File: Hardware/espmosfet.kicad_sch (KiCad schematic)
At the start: 59 parts, among them J1 USB_B_Micro, J2 Conn_01x04_Male, J3 USB_A, J4 Conn_01x04_Male, J5 Conn_01x02_Male, J6 Conn_01x02_Male, J7 Conn_01x03_Male, P1 USB_C_Receptacle_USB2.0, P2 USB_C_Receptacle_USB2.0, Q1 AO3400A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

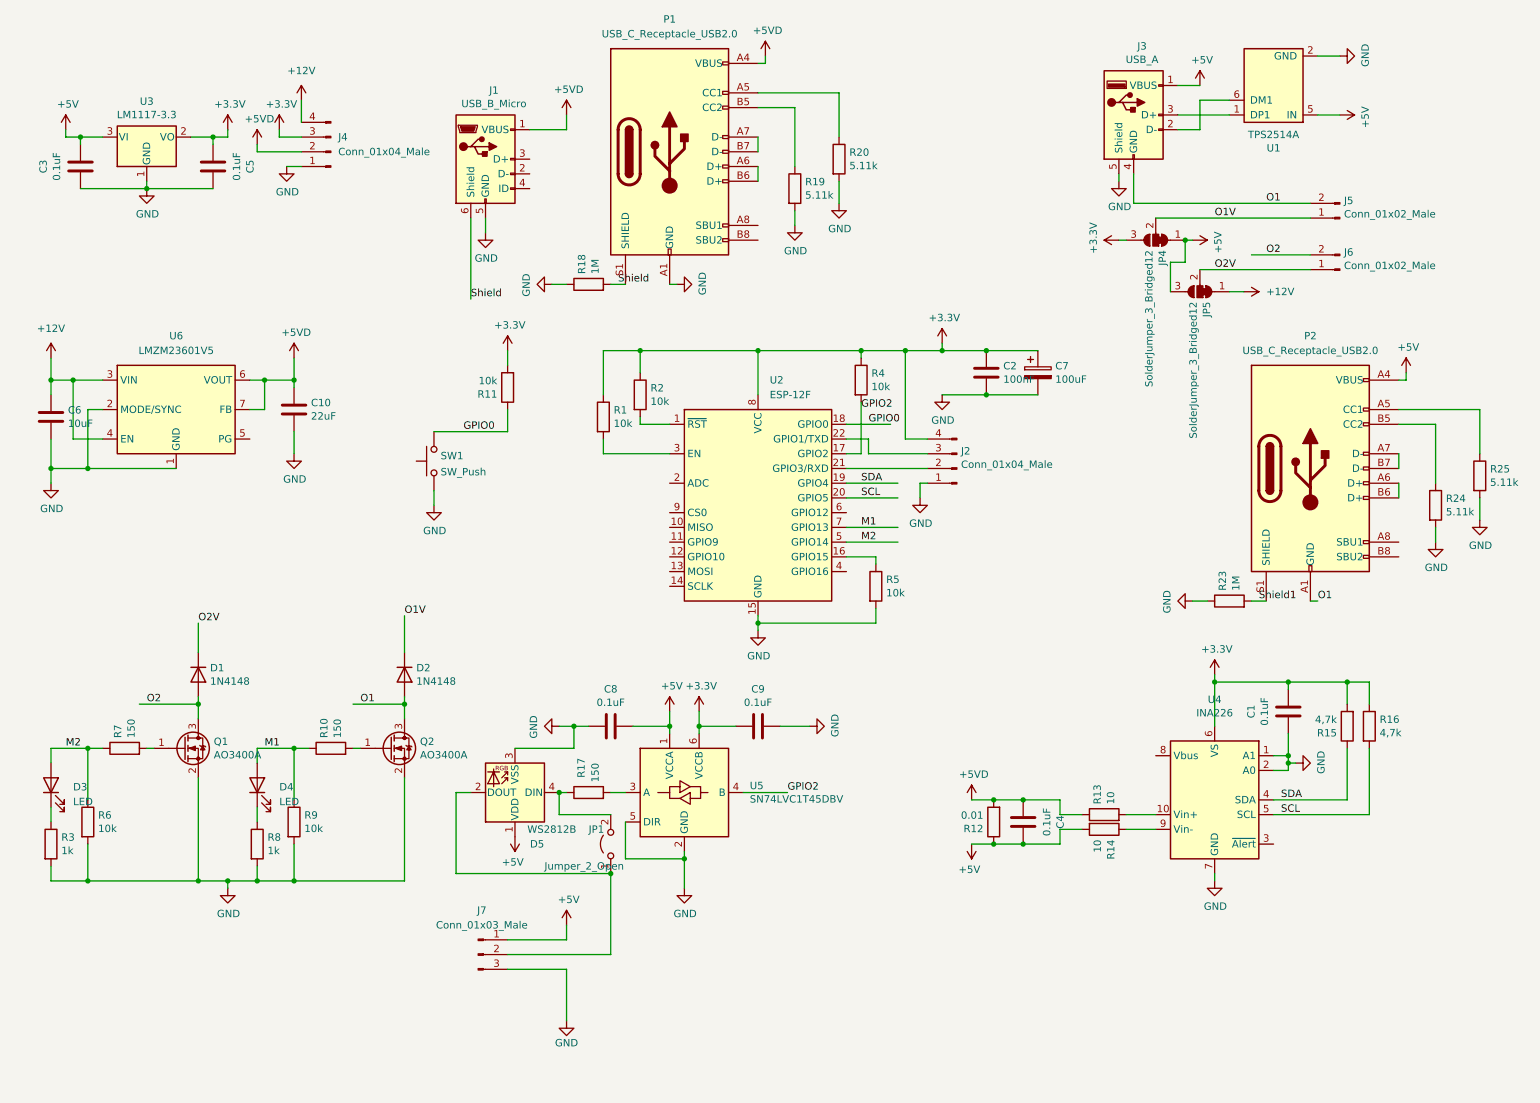
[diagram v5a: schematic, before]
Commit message: fix ws2812b pinout, change to open jumpers
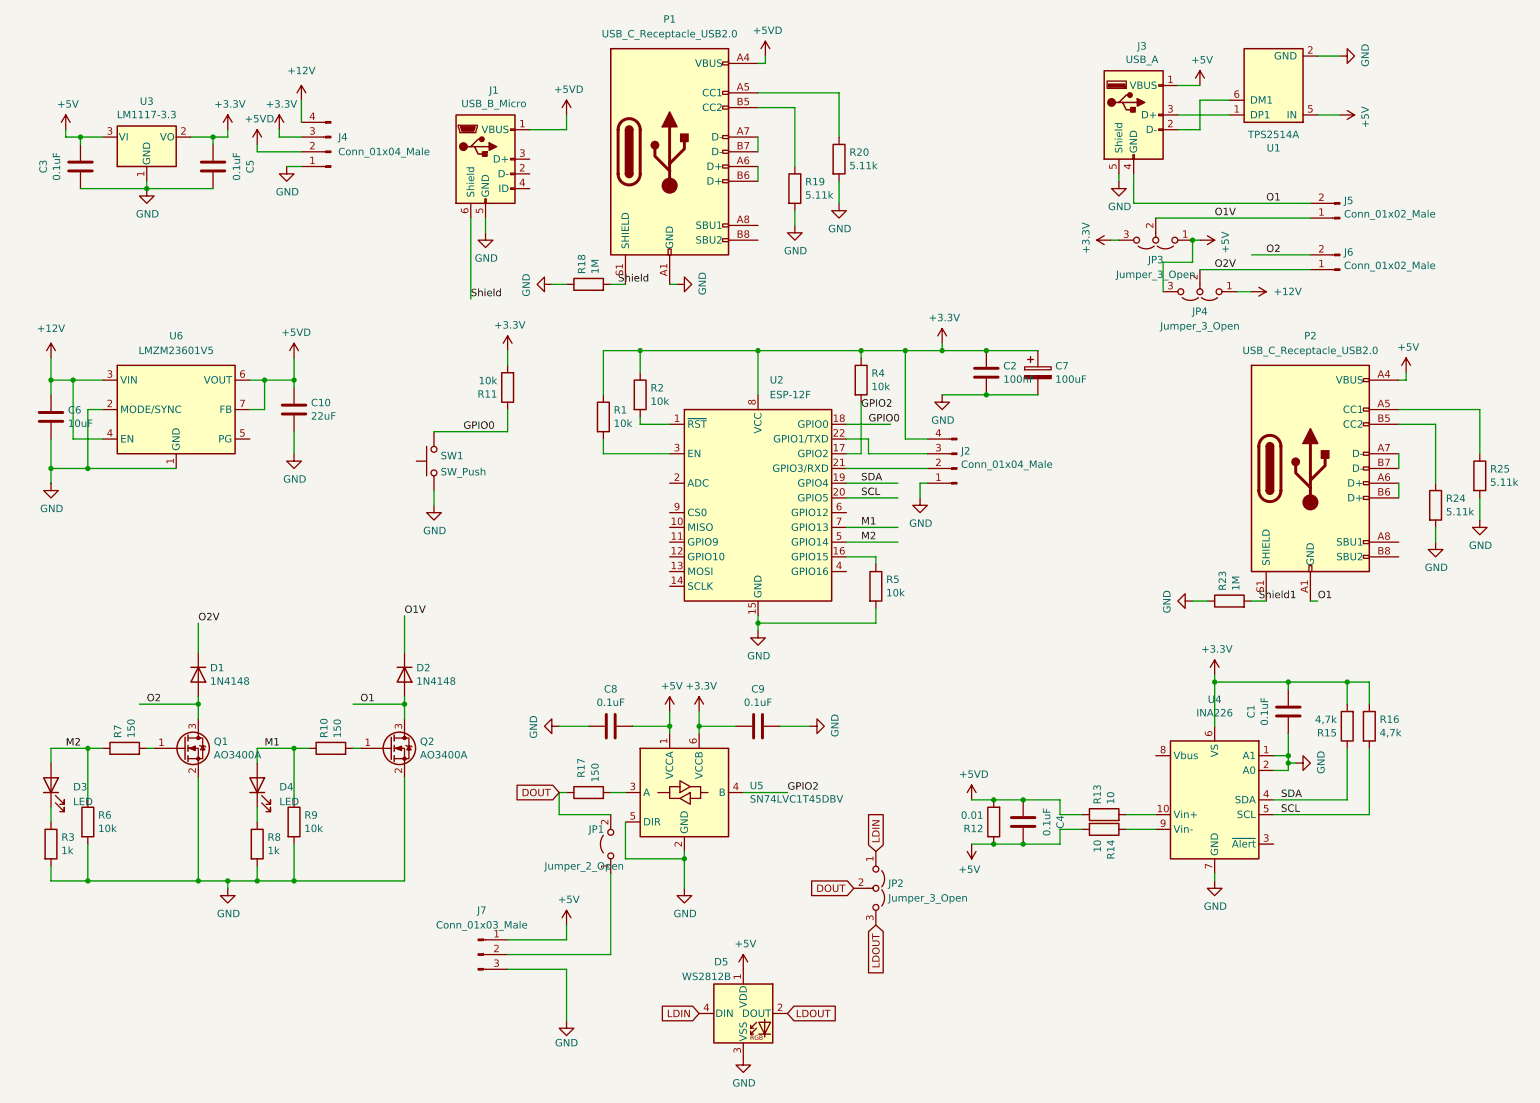
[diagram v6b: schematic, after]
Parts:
- removed JP4, JP5: SolderJumper_3_Bridged12, Jumper:SolderJumper-3_P1.3mm_Bridged12_Pad1.0x1.5mm, symbol Jumper:SolderJumper_3_Bridged12
- added JP2, JP3, JP4: Jumper_3_Open, Jumper:SolderJumper-3_P1.3mm_Open_Pad1.0x1.5mm, symbol Jumper:Jumper_3_Open
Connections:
- net +12V: now also JP4.1 (A)
- net +3V3: now also JP3.3 (B)
- net +5V: now also JP3.1 (A), JP4.3 (B)
- net O1V: now also JP3.2 (C)
- net O2V: now also JP4.2 (C)
- net at J7.2 (Pin_2), JP1.1 (A): no longer D5.2 (DOUT)
- net DOUT: now reaches JP1.2 (B), R17.1
- net DOUT: now also JP2.2 (C); no longer D5.4 (DIN)
- new net LDIN: D5.4 (DIN), JP2.1 (A)
- new net LDOUT: D5.2 (DOUT), JP2.3 (B)
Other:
- moved on the sheet: D5
